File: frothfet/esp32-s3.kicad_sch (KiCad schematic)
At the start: 29 parts, among them J13 USB_TYPE_C_16PIN, J14 Conn_01x04, SW1 BOOT, SW2 RESET, U30 ESP32-S3-WROOM-1-N16R8, U31 USBLC6-2SC6, U32 SN74LV1T34DBV, U33 XC6210B332MR

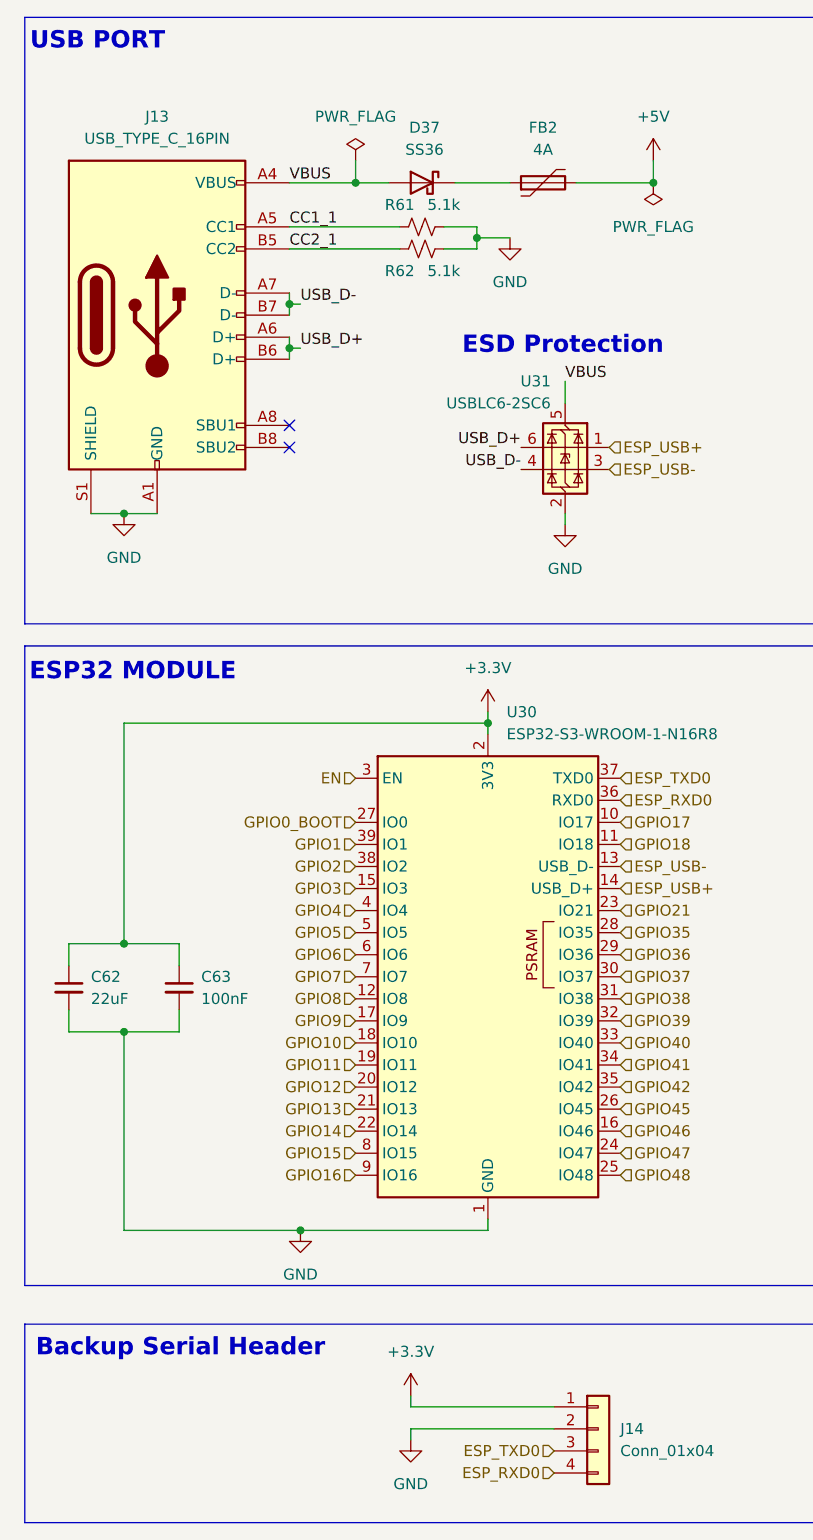
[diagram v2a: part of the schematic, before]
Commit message: rearranged leds and cleaned things up a bit.
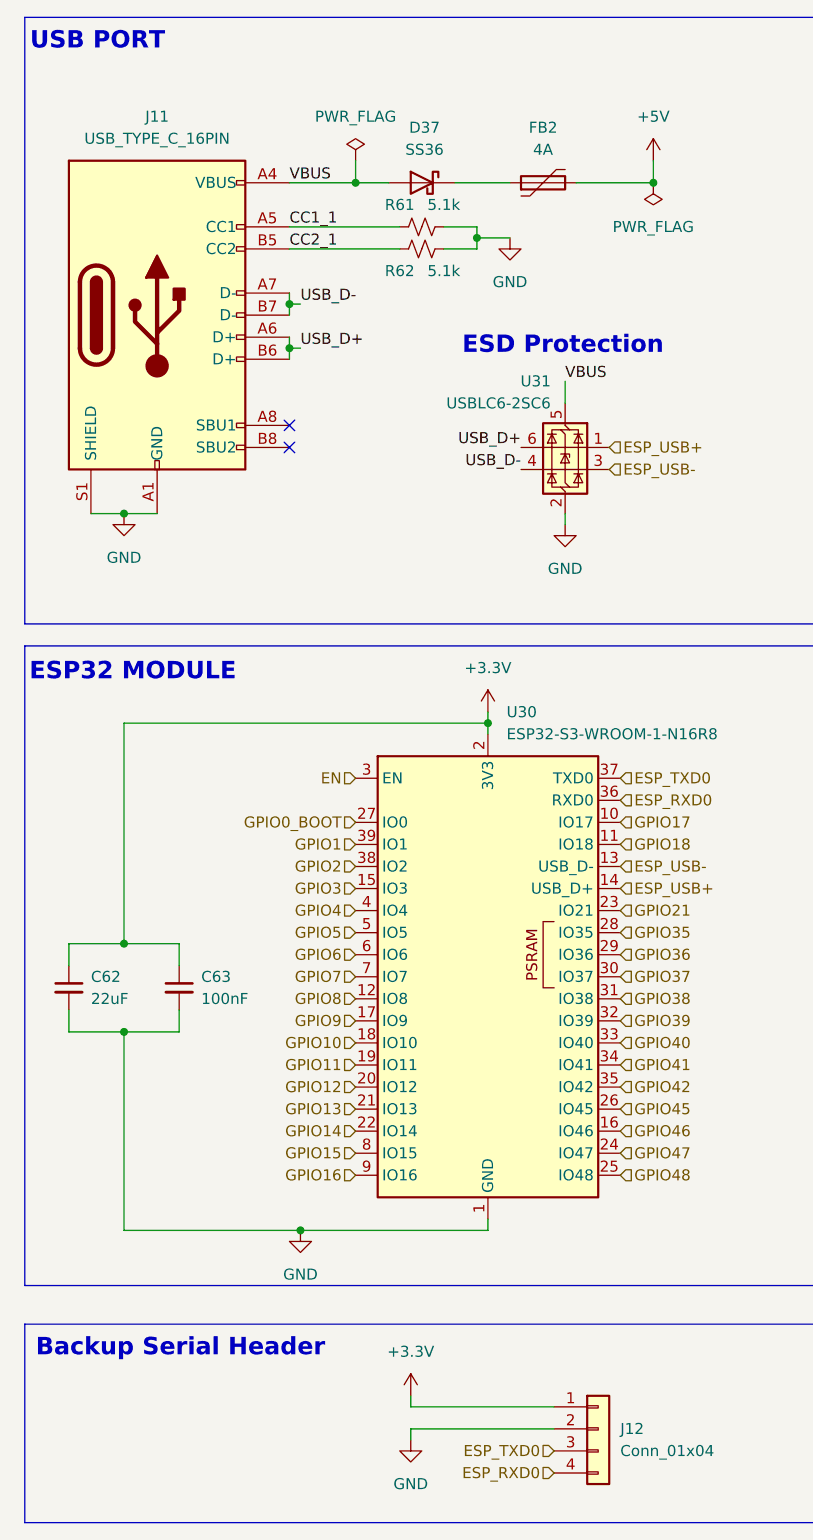
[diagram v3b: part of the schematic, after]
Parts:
- renumbered J13 to J11, J14 to J12
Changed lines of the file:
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@@
 		(on_board yes)
 		(dnp no)
-		(property "Reference" "#PWR0153"
+		(property "Reference" "#PWR0149"
 			(at 97.79 179.07 0)
 			(effects
@@
 			(project "frothfet"
 				(path "/c83c6236-96e9-46ad-9d7a-9e2efa4a7966/777fe0ac-daa5-4cfe-9bd1-5eba0a425019"
-					(reference "#PWR0153")
+					(reference "#PWR0149")
 					(unit 1)
 				)
@@
 		(on_board yes)
 		(dnp no)
-		(property "Reference" "#PWR0165"
+		(property "Reference" "#PWR0161"
 			(at 220.98 119.38 0)
 			(effects
@@
 			(project "frothfet"
 				(path "/c83c6236-96e9-46ad-9d7a-9e2efa4a7966/777fe0ac-daa5-4cfe-9bd1-5eba0a425019"
-					(reference "#PWR0165")
+					(reference "#PWR0161")
 					(unit 1)
 				)
@@
 		(dnp no)
 		(fields_autoplaced yes)
-		(property "Reference" "#PWR0157"
+		(property "Reference" "#PWR0153"
 			(at 115.57 81.28 0)
 			(effects
@@
 			(project "frothfet"
 				(path "/c83c6236-96e9-46ad-9d7a-9e2efa4a7966/777fe0ac-daa5-4cfe-9bd1-5eba0a425019"
-					(reference "#PWR0157")
+					(reference "#PWR0153")
 					(unit 1)
 				)
@@
 		(on_board yes)
 		(dnp no)
-		(property "Reference" "#PWR0159"
+		(property "Reference" "#PWR0155"
 			(at 163.83 31.75 0)
 			(effects
@@
 			(project "frothfet"
 				(path "/c83c6236-96e9-46ad-9d7a-9e2efa4a7966/777fe0ac-daa5-4cfe-9bd1-5eba0a425019"
-					(reference "#PWR0159")
+					(reference "#PWR0155")
 					(unit 1)
 				)
@@
 		(on_board yes)
 		(dnp no)
-		(property "Reference" "#PWR0164"
+		(property "Reference" "#PWR0160"
 			(at 213.36 64.77 0)
 			(effects
@@
 			(project "frothfet"
 				(path "/c83c6236-96e9-46ad-9d7a-9e2efa4a7966/777fe0ac-daa5-4cfe-9bd1-5eba0a425019"
-					(reference "#PWR0164")
+					(reference "#PWR0160")
 					(unit 1)
 				)
@@
 		(dnp no)
 		(fields_autoplaced yes)
-		(property "Reference" "J14"
+		(property "Reference" "J12"
 			(at 121.92 179.0699 0)
 			(effects
@@
 			(project "frothfet"
 				(path "/c83c6236-96e9-46ad-9d7a-9e2efa4a7966/777fe0ac-daa5-4cfe-9bd1-5eba0a425019"
-					(reference "J14")
+					(reference "J12")
 					(unit 1)
 				)
@@
 		(on_board yes)
 		(dnp no)
-		(property "Reference" "#PWR0160"
+		(property "Reference" "#PWR0156"
 			(at 184.15 119.38 0)
 			(effects
@@
 			(project "frothfet"
 				(path "/c83c6236-96e9-46ad-9d7a-9e2efa4a7966/777fe0ac-daa5-4cfe-9bd1-5eba0a425019"
-					(reference "#PWR0160")
+					(reference "#PWR0156")
 					(unit 1)
 				)
@@
 		(dnp no)
 		(fields_autoplaced yes)
-		(property "Reference" "#PWR0154"
+		(property "Reference" "#PWR0150"
 			(at 97.79 186.69 0)
 			(effects
@@
 			(project "frothfet"
 				(path "/c83c6236-96e9-46ad-9d7a-9e2efa4a7966/777fe0ac-daa5-4cfe-9bd1-5eba0a425019"
-					(reference "#PWR0154")
+					(reference "#PWR0150")
 					(unit 1)
 				)
@@
 		(dnp no)
 		(fields_autoplaced yes)
-		(property "Reference" "#PWR0152"
+		(property "Reference" "#PWR0148"
 			(at 85.09 162.56 0)
 			(effects
@@
 			(project "frothfet"
 				(path "/c83c6236-96e9-46ad-9d7a-9e2efa4a7966/777fe0ac-daa5-4cfe-9bd1-5eba0a425019"
-					(reference "#PWR0152")
+					(reference "#PWR0148")
 					(unit 1)
 				)
@@
 		(dnp no)
 		(fields_autoplaced yes)
-		(property "Reference" "#PWR0163"
+		(property "Reference" "#PWR0159"
 			(at 204.47 83.82 0)
 			(effects
@@
 			(project "frothfet"
 				(path "/c83c6236-96e9-46ad-9d7a-9e2efa4a7966/777fe0ac-daa5-4cfe-9bd1-5eba0a425019"
-					(reference "#PWR0163")
+					(reference "#PWR0159")
 					(unit 1)
 				)
@@
 		(dnp no)
 		(fields_autoplaced yes)
-		(property "Reference" "#PWR0167"
+		(property "Reference" "#PWR0163"
 			(at 229.87 144.78 0)
 			(effects
@@
 			(project "frothfet"
 				(path "/c83c6236-96e9-46ad-9d7a-9e2efa4a7966/777fe0ac-daa5-4cfe-9bd1-5eba0a425019"
-					(reference "#PWR0167")
+					(reference "#PWR0163")
 					(unit 1)
 				)
@@
 		(dnp no)
 		(fields_autoplaced yes)
-		(property "Reference" "#PWR0161"
+		(property "Reference" "#PWR0157"
 			(at 193.04 143.51 0)
 			(effects
@@
 			(project "frothfet"
 				(path "/c83c6236-96e9-46ad-9d7a-9e2efa4a7966/777fe0ac-daa5-4cfe-9bd1-5eba0a425019"
-					(reference "#PWR0161")
+					(reference "#PWR0157")
 					(unit 1)
 				)
@@
 		(dnp no)
 		(fields_autoplaced yes)
-		(property "Reference" "#PWR0156"
+		(property "Reference" "#PWR0152"
 			(at 109.22 48.26 0)
 			(effects
@@
 			(project "frothfet"
 				(path "/c83c6236-96e9-46ad-9d7a-9e2efa4a7966/777fe0ac-daa5-4cfe-9bd1-5eba0a425019"
-					(reference "#PWR0156")
+					(reference "#PWR0152")
 					(unit 1)
 				)
@@
 		(on_board yes)
 		(dnp no)
-		(property "Reference" "#PWR0155"
+		(property "Reference" "#PWR0151"
 			(at 106.68 100.33 0)
 			(effects
@@
 			(project "frothfet"
 				(path "/c83c6236-96e9-46ad-9d7a-9e2efa4a7966/777fe0ac-daa5-4cfe-9bd1-5eba0a425019"
-					(reference "#PWR0155")
+					(reference "#PWR0151")
 					(unit 1)
 				)
@@
 		(dnp no)
 		(fields_autoplaced yes)
-		(property "Reference" "J13"
+		(property "Reference" "J11"
 			(at 68.58 27.94 0)
 			(effects
@@
 			(project "frothfet"
 				(path "/c83c6236-96e9-46ad-9d7a-9e2efa4a7966/777fe0ac-daa5-4cfe-9bd1-5eba0a425019"
-					(reference "J13")
+					(reference "J11")
 					(unit 1)
 				)
@@
 		(on_board yes)
 		(dnp no)
-		(property "Reference" "#PWR0166"
+		(property "Reference" "#PWR0162"
 			(at 228.6 31.75 0)
 			(effects
@@
 			(project "frothfet"
 				(path "/c83c6236-96e9-46ad-9d7a-9e2efa4a7966/777fe0ac-daa5-4cfe-9bd1-5eba0a425019"
-					(reference "#PWR0166")
+					(reference "#PWR0162")
 					(unit 1)
 				)
@@
 		(dnp no)
 		(fields_autoplaced yes)
-		(property "Reference" "#PWR0151"
+		(property "Reference" "#PWR0147"
 			(at 64.77 80.01 0)
 			(effects
@@
 			(project "frothfet"
 				(path "/c83c6236-96e9-46ad-9d7a-9e2efa4a7966/777fe0ac-daa5-4cfe-9bd1-5eba0a425019"
-					(reference "#PWR0151")
+					(reference "#PWR0147")
 					(unit 1)
 				)
@@
 		(on_board yes)
 		(dnp no)
-		(property "Reference" "#PWR0158"
+		(property "Reference" "#PWR0154"
 			(at 125.73 36.83 0)
 			(effects
@@
 			(project "frothfet"
 				(path "/c83c6236-96e9-46ad-9d7a-9e2efa4a7966/777fe0ac-daa5-4cfe-9bd1-5eba0a425019"
-					(reference "#PWR0158")
+					(reference "#PWR0154")
 					(unit 1)
 				)
@@
 		(dnp no)
 		(fields_autoplaced yes)
-		(property "Reference" "#PWR0162"
+		(property "Reference" "#PWR0158"
 			(at 201.93 48.26 0)
 			(effects
@@
 			(project "frothfet"
 				(path "/c83c6236-96e9-46ad-9d7a-9e2efa4a7966/777fe0ac-daa5-4cfe-9bd1-5eba0a425019"
-					(reference "#PWR0162")
+					(reference "#PWR0158")
 					(unit 1)
 				)

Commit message: working on bom
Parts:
- J5: renamed from J12; footprint Connector_PinHeader_2.54mm:PinHeader_1x04_P2.54mm_Vertical_SMD_Pin1Left -> Connector_PinHeader_2.54mm:PinHeader_1x04_P2.54mm_Vertical_SMD_Pin1Right
- renumbered J11 to J4
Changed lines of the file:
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@@
 		(dnp no)
 		(fields_autoplaced yes)
-		(property "Reference" "J12"
+		(property "Reference" "J5"
 			(at 121.92 179.0699 0)
 			(effects
@@
 			)
 		)
-		(property "Footprint" "Connector_PinHeader_2.54mm:PinHeader_1x04_P2.54mm_Vertical_SMD_Pin1Left"
+		(property "Footprint" "Connector_PinHeader_2.54mm:PinHeader_1x04_P2.54mm_Vertical_SMD_Pin1Right"
 			(at 119.38 179.07 0)
 			(effects
@@
 			(project "frothfet"
 				(path "/c83c6236-96e9-46ad-9d7a-9e2efa4a7966/777fe0ac-daa5-4cfe-9bd1-5eba0a425019"
-					(reference "J12")
+					(reference "J5")
 					(unit 1)
 				)
@@
 		(dnp no)
 		(fields_autoplaced yes)
-		(property "Reference" "J11"
+		(property "Reference" "J4"
 			(at 68.58 27.94 0)
 			(effects
@@
 			(project "frothfet"
 				(path "/c83c6236-96e9-46ad-9d7a-9e2efa4a7966/777fe0ac-daa5-4cfe-9bd1-5eba0a425019"
-					(reference "J11")
+					(reference "J4")
 					(unit 1)
 				)

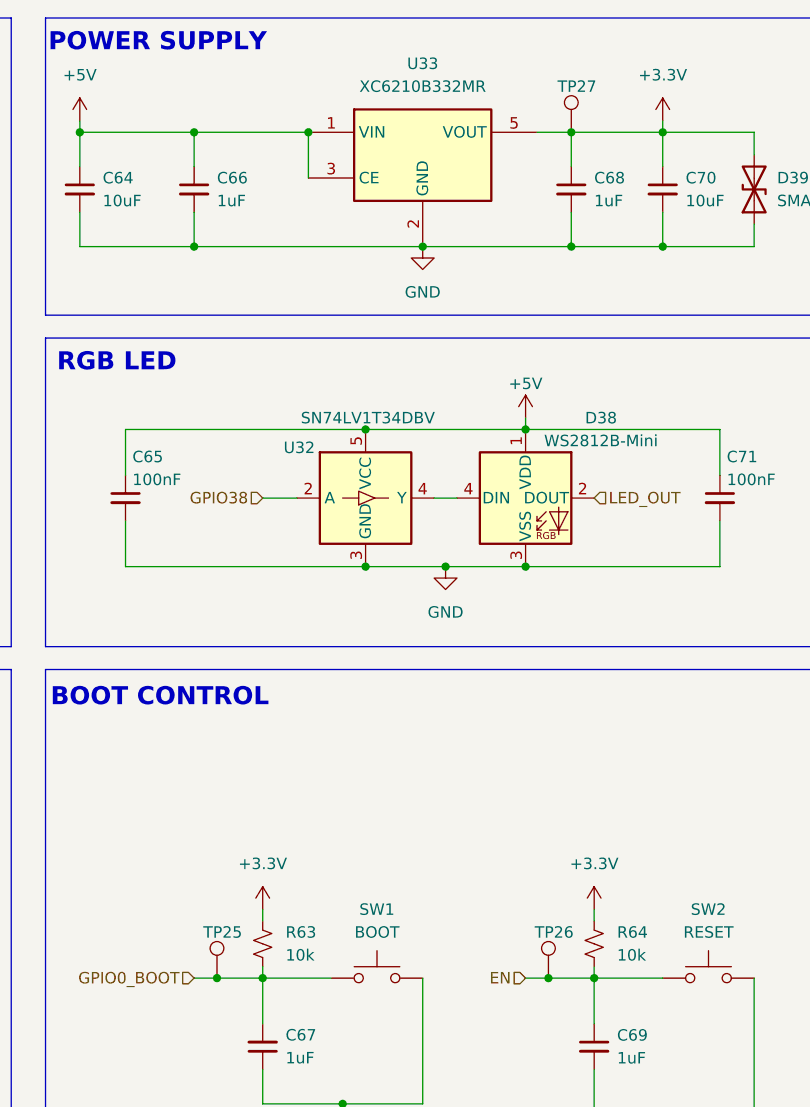
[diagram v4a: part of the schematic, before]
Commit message: changed to XFCN 508 because 507 wasnt available on jlc
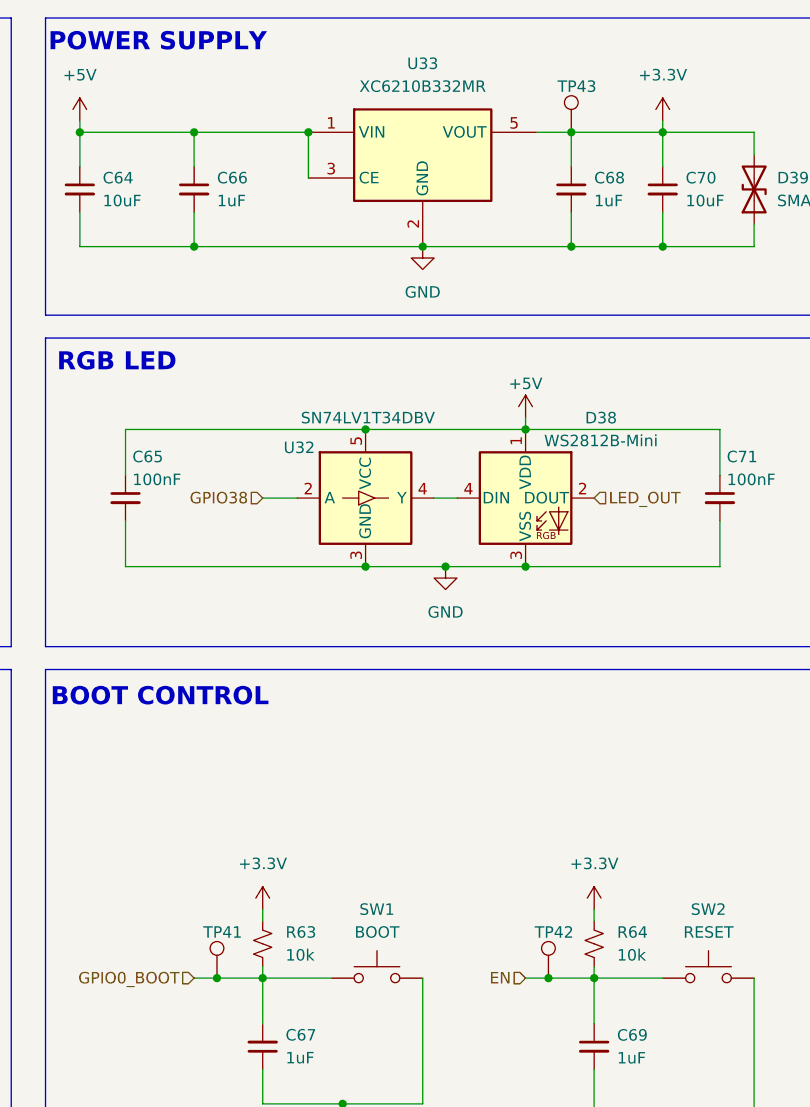
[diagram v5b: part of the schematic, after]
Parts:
- renumbered TP25 to TP41, TP26 to TP42, TP27 to TP43
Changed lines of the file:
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@@
 		(on_board yes)
 		(dnp no)
-		(property "Reference" "TP27"
+		(property "Reference" "TP43"
 			(at 216.916 24.13 0)
 			(effects
@@
 			(project "frothfet"
 				(path "/c83c6236-96e9-46ad-9d7a-9e2efa4a7966/777fe0ac-daa5-4cfe-9bd1-5eba0a425019"
-					(reference "TP27")
+					(reference "TP43")
 					(unit 1)
 				)
@@
 		(on_board yes)
 		(dnp no)
-		(property "Reference" "TP26"
+		(property "Reference" "TP42"
 			(at 214.376 118.11 0)
 			(effects
@@
 			(project "frothfet"
 				(path "/c83c6236-96e9-46ad-9d7a-9e2efa4a7966/777fe0ac-daa5-4cfe-9bd1-5eba0a425019"
-					(reference "TP26")
+					(reference "TP42")
 					(unit 1)
 				)
@@
 		(on_board yes)
 		(dnp no)
-		(property "Reference" "TP25"
+		(property "Reference" "TP41"
 			(at 177.546 118.11 0)
 			(effects
@@
 			(project "frothfet"
 				(path "/c83c6236-96e9-46ad-9d7a-9e2efa4a7966/777fe0ac-daa5-4cfe-9bd1-5eba0a425019"
-					(reference "TP25")
-					(unit 1)
-				)
+					(reference "TP41")
+					(unit 1)
+				)

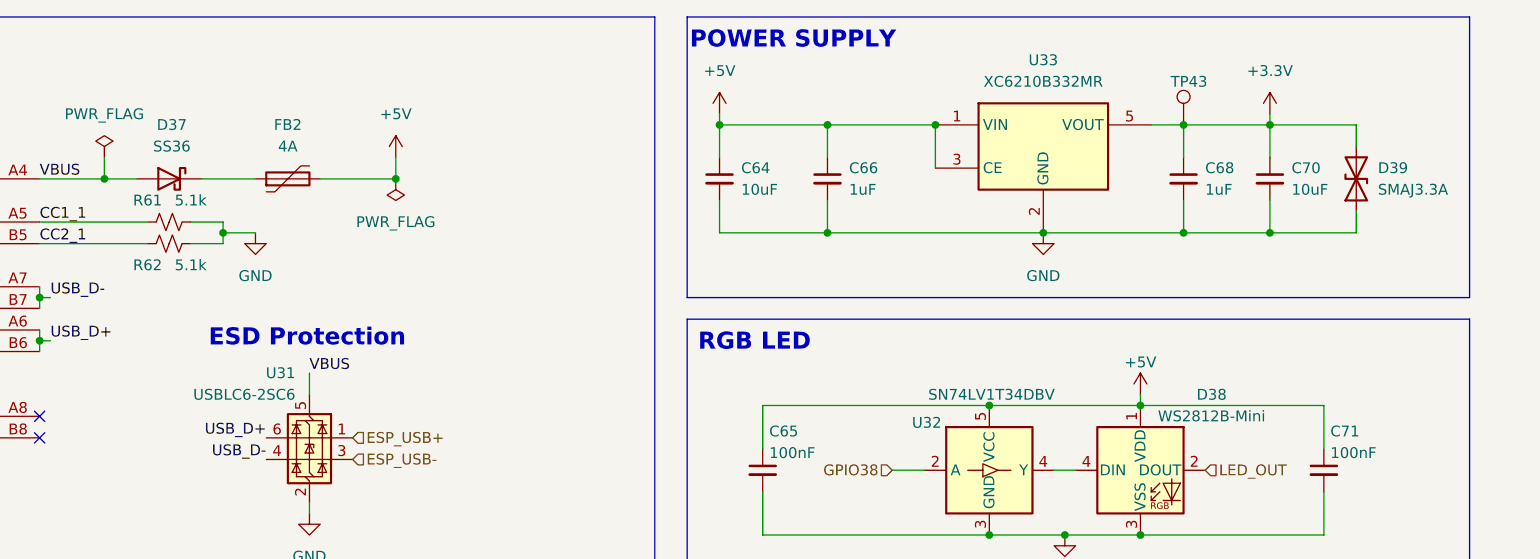
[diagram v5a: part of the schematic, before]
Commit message: add esd protection to each channel output
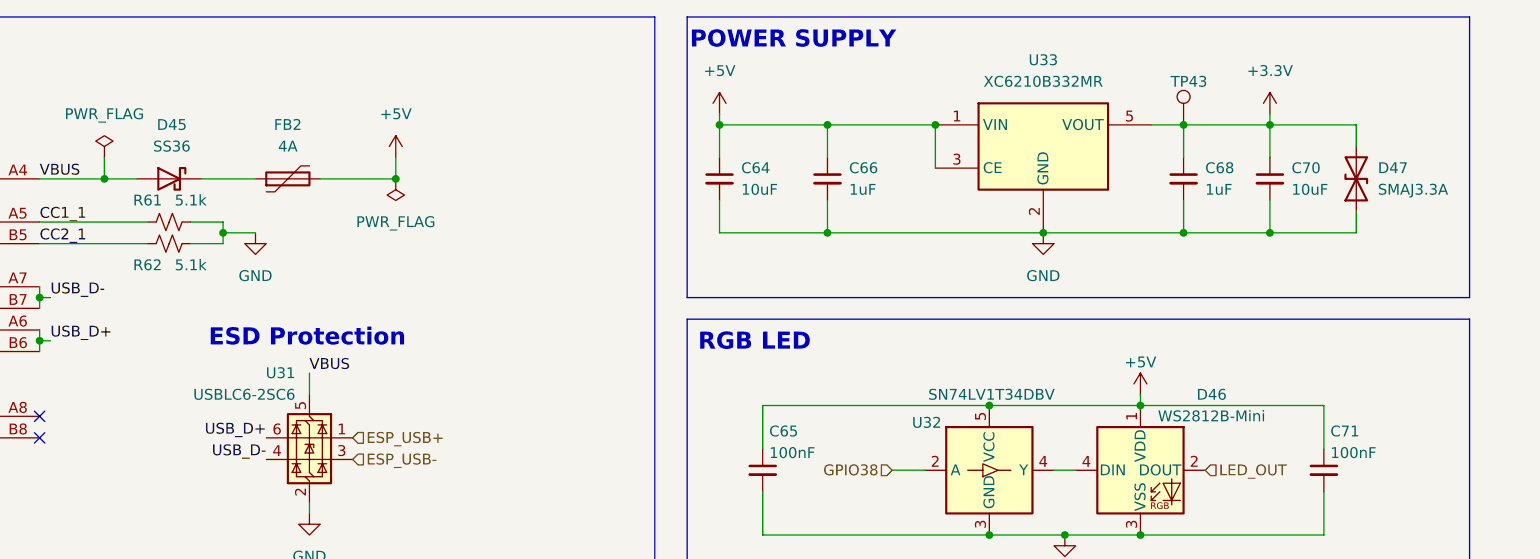
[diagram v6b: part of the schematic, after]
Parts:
- renumbered D37 to D45, D38 to D46, D39 to D47
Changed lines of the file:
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@@
 		(on_board yes)
 		(dnp no)
-		(property "Reference" "D39"
+		(property "Reference" "D47"
 			(at 241.3 34.29 90)
 			(effects
@@
 			(project "frothfet"
 				(path "/c83c6236-96e9-46ad-9d7a-9e2efa4a7966/777fe0ac-daa5-4cfe-9bd1-5eba0a425019"
-					(reference "D39")
+					(reference "D47")
 					(unit 1)
 				)
@@
 		(on_board yes)
 		(dnp no)
-		(property "Reference" "D37"
+		(property "Reference" "D45"
 			(at 99.3775 29.21 0)
 			(effects
@@
 			(project "frothfet"
 				(path "/c83c6236-96e9-46ad-9d7a-9e2efa4a7966/777fe0ac-daa5-4cfe-9bd1-5eba0a425019"
-					(reference "D37")
+					(reference "D45")
 					(unit 1)
 				)
@@
 		(on_board yes)
 		(dnp no)
-		(property "Reference" "D38"
+		(property "Reference" "D46"
 			(at 221.742 60.96 0)
 			(effects
@@
 			(project "frothfet"
 				(path "/c83c6236-96e9-46ad-9d7a-9e2efa4a7966/777fe0ac-daa5-4cfe-9bd1-5eba0a425019"
-					(reference "D38")
-					(unit 1)
-				)
+					(reference "D46")
+					(unit 1)
+				)
